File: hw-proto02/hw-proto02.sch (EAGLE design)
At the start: 25 parts, among them IC1 VN5E160MSTR-E, IC3 MCP2562T, IC5 IR4427S, J1 000, J2 000, Q1 SQJ147ELP-T1_GE3, Q2 SQJ147ELP-T1_GE3

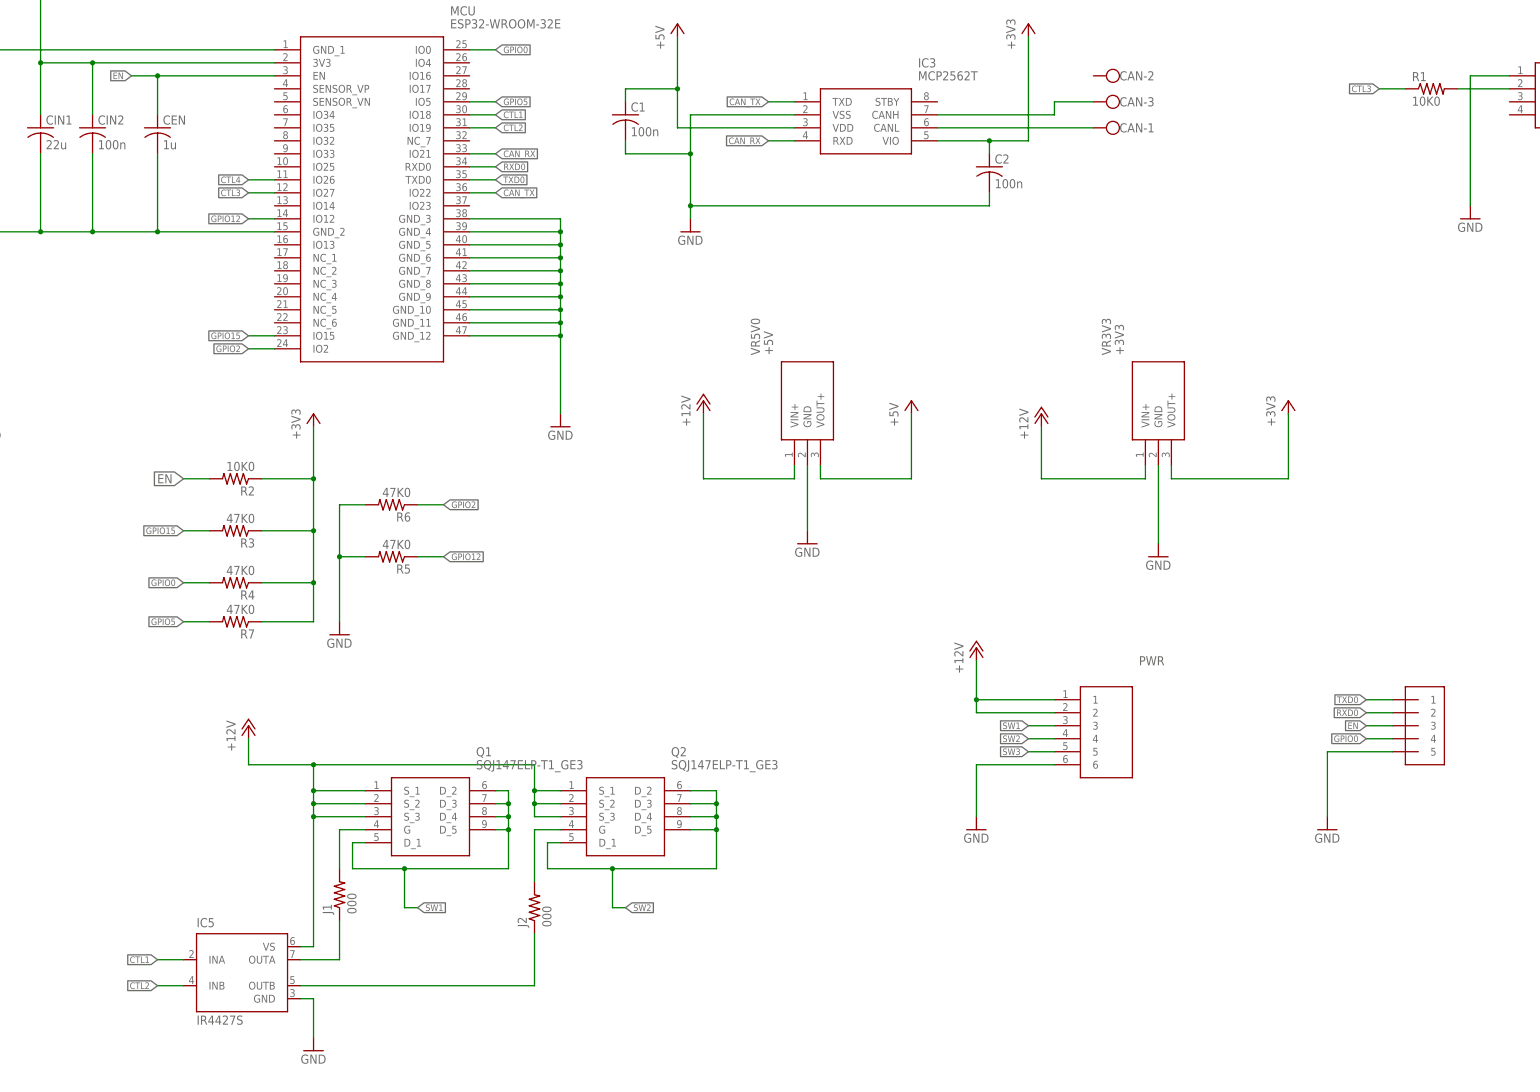
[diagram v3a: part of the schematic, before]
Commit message: updated mosfet driver
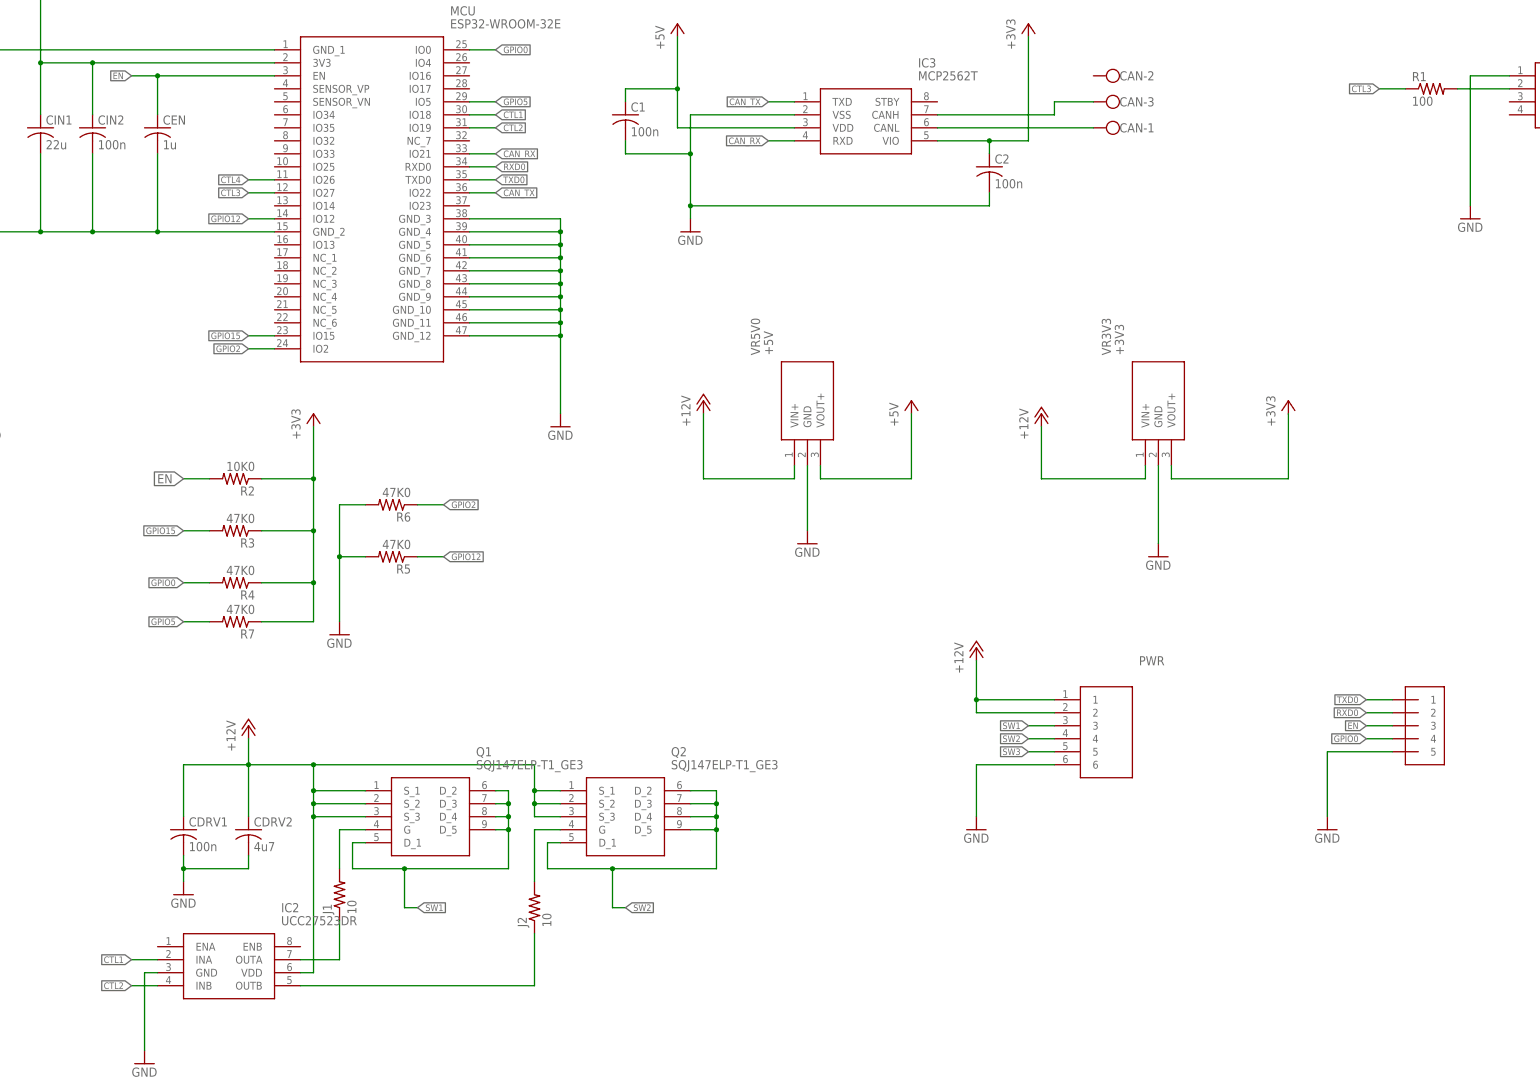
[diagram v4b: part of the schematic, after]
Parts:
- removed IC5: IR4427S, ir:IR4427S
- added CDRV1: 100n, rcl:C-USC0603K
- added CDRV2: 4u7, rcl:C-USC0805K
- added IC2: UCC27523DR, UCC27523DR-fet-driver:UCC27523DR
- J1, J2: value 000 -> 10
- R1: value 10K0 -> 100
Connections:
- net +12V: now also CDRV1.1, CDRV2.1, IC2.VDD; no longer IC5.VS
- net CTL1: now also IC2.INA; no longer IC5.INA
- net CTL2: now also IC2.INB; no longer IC5.INB
- net GND: now also CDRV1.2, CDRV2.2, IC2.GND; no longer IC5.GND
- net N$3: now also IC2.OUTB; no longer IC5.OUTB
- net N$4: now also IC2.OUTA; no longer IC5.OUTA
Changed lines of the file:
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@@
 <part name="CAN" library="con-wago-500" deviceset="W237-103" device=""/>
 <part name="P+7" library="supply1" deviceset="+12V" device=""/>
-<part name="IC5" library="ir" deviceset="IR4427" device="S"/>
 <part name="GND9" library="supply1" deviceset="GND" device=""/>
-<part name="J1" library="rcl" deviceset="R-US_" device="0204/7" value="000"/>
-<part name="J2" library="rcl" deviceset="R-US_" device="0204/7" value="000"/>
-<part name="R1" library="rcl" deviceset="R-US_" device="0204/7" value="10K0"/>
+<part name="J1" library="rcl" deviceset="R-US_" device="0204/7" value="10"/>
+<part name="J2" library="rcl" deviceset="R-US_" device="0204/7" value="10"/>
+<part name="R1" library="rcl" deviceset="R-US_" device="0204/7" value="100"/>
 <part name="C1" library="rcl" deviceset="C-US" device="C0603K" value="100n"/>
 <part name="C2" library="rcl" deviceset="C-US" device="C0603K" value="100n"/>
@@
 <part name="CIN2" library="rcl" deviceset="C-US" device="C0603K" value="100n"/>
 <part name="CEN" library="rcl" deviceset="C-US" device="C0603K" value="1u"/>
+<part name="IC2" library="UCC27523DR-fet-driver" deviceset="UCC27523DR" device=""/>
+<part name="CDRV2" library="rcl" deviceset="C-US" device="C0805K" value="4u7"/>
+<part name="CDRV1" library="rcl" deviceset="C-US" device="C0603K" value="100n"/>
+<part name="GND3" library="supply1" deviceset="GND" device=""/>
 </parts>
 <sheets>
@@
 <instance part="CAN" gate="-3" x="160.02" y="215.9" rot="R180"/>
 <instance part="P+7" gate="1" x="276.86" y="243.84"/>
-<instance part="IC5" gate="P" x="-12.7" y="45.72"/>
-<instance part="GND9" gate="1" x="2.54" y="30.48"/>
+<instance part="GND9" gate="1" x="-30.48" y="27.94"/>
 <instance part="J1" gate="G$1" x="7.62" y="60.96" rot="R90"/>
 <instance part="J2" gate="G$1" x="45.72" y="58.42" rot="R90"/>
@@
 <instance part="CIN2" gate="G$1" x="-40.64" y="210.82"/>
 <instance part="CEN" gate="G$1" x="-27.94" y="210.82"/>
+<instance part="IC2" gate="G$1" x="-27.94" y="50.8"/>
+<instance part="CDRV2" gate="G$1" x="-10.16" y="73.66"/>
+<instance part="CDRV1" gate="G$1" x="-22.86" y="73.66"/>
+<instance part="GND3" gate="1" x="-22.86" y="60.96"/>
 </instances>
 <busses>
@@
 </segment>
 <segment>
-<pinref part="IC5" gate="P" pin="GND"/>
 <pinref part="GND9" gate="1" pin="GND"/>
-<wire x1="0" y1="40.64" x2="2.54" y2="40.64" width="0.1524" layer="91"/>
-<wire x1="2.54" y1="40.64" x2="2.54" y2="33.02" width="0.1524" layer="91"/>
+<wire x1="-27.94" y1="45.72" x2="-30.48" y2="45.72" width="0.1524" layer="91"/>
+<wire x1="-30.48" y1="45.72" x2="-30.48" y2="30.48" width="0.1524" layer="91"/>
+<pinref part="IC2" gate="G$1" pin="GND"/>
 </segment>
 <segment>
@@
 <wire x1="213.36" y1="88.9" x2="200.66" y2="88.9" width="0.1524" layer="91"/>
 <wire x1="200.66" y1="88.9" x2="200.66" y2="76.2" width="0.1524" layer="91"/>
+</segment>
+<segment>
+<pinref part="CDRV1" gate="G$1" pin="2"/>
+<pinref part="GND3" gate="1" pin="GND"/>
+<wire x1="-22.86" y1="68.58" x2="-22.86" y2="66.04" width="0.1524" layer="91"/>
+<pinref part="CDRV2" gate="G$1" pin="2"/>
+<wire x1="-22.86" y1="66.04" x2="-22.86" y2="63.5" width="0.1524" layer="91"/>
+<wire x1="-22.86" y1="66.04" x2="-10.16" y2="66.04" width="0.1524" layer="91"/>
+<wire x1="-10.16" y1="66.04" x2="-10.16" y2="68.58" width="0.1524" layer="91"/>
+<junction x="-22.86" y="66.04"/>
 </segment>
 </net>
@@
 <wire x1="2.54" y1="86.36" x2="-10.16" y2="86.36" width="0.1524" layer="91"/>
 <pinref part="P+1" gate="1" pin="+12V"/>
-<pinref part="IC5" gate="P" pin="VS"/>
-<wire x1="0" y1="50.8" x2="2.54" y2="50.8" width="0.1524" layer="91"/>
-<wire x1="2.54" y1="50.8" x2="2.54" y2="76.2" width="0.1524" layer="91"/>
+<wire x1="0" y1="45.72" x2="2.54" y2="45.72" width="0.1524" layer="91"/>
+<wire x1="2.54" y1="45.72" x2="2.54" y2="76.2" width="0.1524" layer="91"/>
 <junction x="2.54" y="86.36"/>
 <pinref part="Q1" gate="G$1" pin="S_3"/>
@@
 <wire x1="45.72" y1="76.2" x2="45.72" y2="78.74" width="0.1524" layer="91"/>
 <junction x="45.72" y="78.74"/>
+<pinref part="IC2" gate="G$1" pin="VDD"/>
+<pinref part="CDRV1" gate="G$1" pin="1"/>
+<wire x1="-10.16" y1="86.36" x2="-22.86" y2="86.36" width="0.1524" layer="91"/>
+<wire x1="-22.86" y1="86.36" x2="-22.86" y2="76.2" width="0.1524" layer="91"/>
+<junction x="-10.16" y="86.36"/>
+<pinref part="CDRV2" gate="G$1" pin="1"/>
+<wire x1="-10.16" y1="76.2" x2="-10.16" y2="86.36" width="0.1524" layer="91"/>
 </segment>
 <segment>
@@
 <net name="N$3" class="0">
 <segment>
-<pinref part="IC5" gate="P" pin="OUTB"/>
 <wire x1="0" y1="43.18" x2="45.72" y2="43.18" width="0.1524" layer="91"/>
 <pinref part="J2" gate="G$1" pin="1"/>
 <wire x1="45.72" y1="43.18" x2="45.72" y2="53.34" width="0.1524" layer="91"/>
+<pinref part="IC2" gate="G$1" pin="OUTB"/>
 </segment>
 </net>
 <net name="N$4" class="0">
 <segment>
-<pinref part="IC5" gate="P" pin="OUTA"/>
 <wire x1="0" y1="48.26" x2="7.62" y2="48.26" width="0.1524" layer="91"/>
 <pinref part="J1" gate="G$1" pin="1"/>
 <wire x1="7.62" y1="48.26" x2="7.62" y2="55.88" width="0.1524" layer="91"/>
+<pinref part="IC2" gate="G$1" pin="OUTA"/>
 </segment>
 </net>
 <net name="CTL2" class="0">
 <segment>
-<pinref part="IC5" gate="P" pin="INB"/>
-<wire x1="-27.94" y1="43.18" x2="-22.86" y2="43.18" width="0.1524" layer="91"/>
-<label x="-27.94" y="43.18" size="1.27" layer="95" rot="R180" xref="yes"/>
+<wire x1="-33.02" y1="43.18" x2="-27.94" y2="43.18" width="0.1524" layer="91"/>
+<label x="-33.02" y="43.18" size="1.27" layer="95" rot="R180" xref="yes"/>
+<pinref part="IC2" gate="G$1" pin="INB"/>
 </segment>
 <segment>
@@
 <net name="CTL1" class="0">
 <segment>
-<pinref part="IC5" gate="P" pin="INA"/>
-<wire x1="-27.94" y1="48.26" x2="-22.86" y2="48.26" width="0.1524" layer="91"/>
-<label x="-27.94" y="48.26" size="1.27" layer="95" rot="R180" xref="yes"/>
-</segment>
-<segment>
+<wire x1="-33.02" y1="48.26" x2="-27.94" y2="48.26" width="0.1524" layer="91"/>
+<label x="-33.02" y="48.26" size="1.27" layer="95" rot="R180" xref="yes"/>
+<pinref part="IC2" gate="G$1" pin="INA"/>
+</segment>
+<segment>

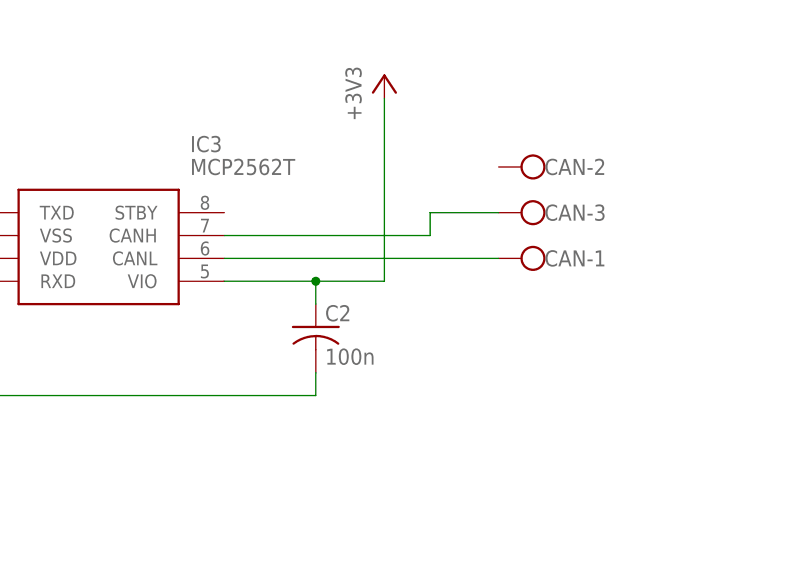
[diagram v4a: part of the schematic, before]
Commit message: grounded can connector, layout tweaks
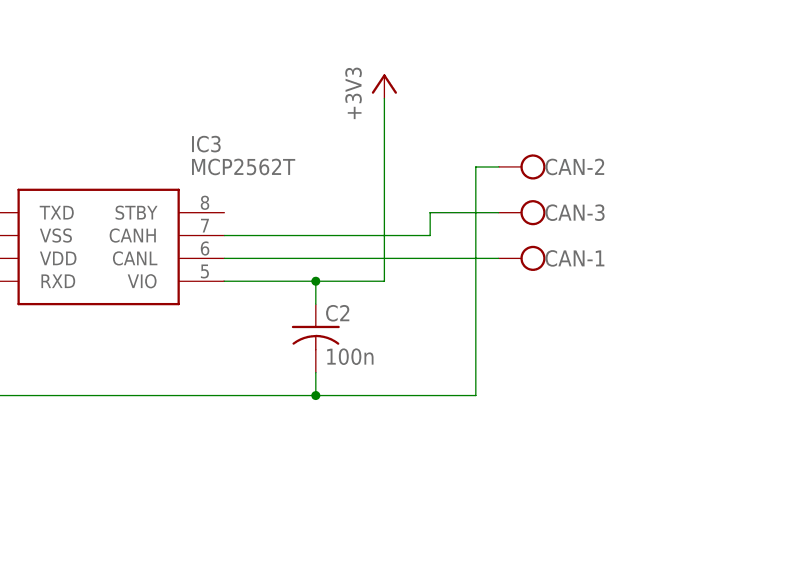
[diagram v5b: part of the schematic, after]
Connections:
- net GND: now also CAN-2.KL
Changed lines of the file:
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@@
 <wire x1="134.62" y1="195.58" x2="76.2" y2="195.58" width="0.1524" layer="91"/>
 <junction x="76.2" y="195.58"/>
+<pinref part="CAN" gate="-2" pin="KL"/>
+<wire x1="154.94" y1="220.98" x2="152.4" y2="220.98" width="0.1524" layer="91"/>
+<wire x1="152.4" y1="220.98" x2="152.4" y2="195.58" width="0.1524" layer="91"/>
+<wire x1="152.4" y1="195.58" x2="134.62" y2="195.58" width="0.1524" layer="91"/>
+<junction x="134.62" y="195.58"/>
 </segment>
 <segment>
